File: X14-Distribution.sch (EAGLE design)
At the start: 55 parts, among them Q1 310mA/60V/1.6Ω, Q2 IRF1018EPBF, Q3 IRF1018EPBF, Q4 IRF1018EPBF, Q5 IRLML5203, Q6 IRLML5203, Q7 IRLML5203, Q8 IRLML5203, U1 DIST_OR_CONTROL_ALTMK06A-M, U2 DIST_OR_CONTROL_ALTMK06A-M

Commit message: Changed the Backplane Logic connector
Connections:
- net +12V: no longer U$1.VIN+
- net +12V_CONV: now also BACKPLANE.12V, U$1.VIN+
- net 12V_GND: now also BACKPLANE.GND_12V
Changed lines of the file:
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@@
 <part name="R12" library="SparkFun-Resistors" library_urn="urn:adsk.eagle:library:532" deviceset="RESISTOR" device="0603" package3d_urn="urn:adsk.eagle:package:39650/1" value="10k"/>
 <part name="R13" library="SparkFun-Resistors" library_urn="urn:adsk.eagle:library:532" deviceset="RESISTOR" device="0603" package3d_urn="urn:adsk.eagle:package:39650/1" value="10k"/>
-<part name="BACKPLANE" library="CONN, Distribution-Backplane" deviceset="DISTRIBUTION-BACKPLANE" device=""/>
 <part name="BRICKS1" library="CONN_Distribution-Bricks" deviceset="PETC-02-40-02-01-X-VT(DTOB)" device=""/>
 <part name="BRICKS2" library="CONN_Distribution-Bricks" deviceset="PETC-02-40-02-01-X-VT(DTOB)" device=""/>
@@
 <part name="Q7" library="Transistor" library_urn="urn:adsk.eagle:library:16378713" deviceset="PMOSFET_" device="" package3d_urn="urn:adsk.eagle:package:28738/2" technology="IRLML5203" value="IRLML5203"/>
 <part name="Q8" library="Transistor" library_urn="urn:adsk.eagle:library:16378713" deviceset="PMOSFET_" device="" package3d_urn="urn:adsk.eagle:package:28738/2" technology="IRLML5203" value="IRLML5203"/>
+<part name="BACKPLANE" library="CONN, Distribution-Backplane" deviceset="DISTRIBUTION-BACKPLANE" device="" value=""/>
 </parts>
 <sheets>
@@
 <attribute name="VALUE" x="410.972" y="-129.286" size="1.778" layer="96" font="vector" rot="R90" align="top-center"/>
 </instance>
-<instance part="BACKPLANE" gate="G$1" x="375.158" y="-151.638" smashed="yes">
-<attribute name="NAME" x="366.014" y="-143.002" size="1.778" layer="95"/>
-</instance>
 <instance part="BRICKS1" gate="G$1" x="88.646" y="-138.176" smashed="yes">
 <attribute name="NAME" x="75.946" y="-125.476" size="1.778" layer="95"/>
@@
 <attribute name="NAME" x="261.112" y="82.55" size="1.778" layer="95"/>
 <attribute name="VALUE" x="261.112" y="80.01" size="1.778" layer="96"/>
+</instance>
+<instance part="BACKPLANE" gate="G$1" x="373.634" y="-153.162" smashed="yes">
+<attribute name="NAME" x="363.474" y="-141.732" size="1.778" layer="95"/>
+<attribute name="VALUE" x="363.474" y="-164.592" size="1.778" layer="96" align="top-left"/>
 </instance>
 </instances>
@@
 <label x="442.468" y="81.788" size="1.27" layer="95" xref="yes"/>
 </segment>
-<segment>
-<pinref part="U$1" gate="G$1" pin="VIN+"/>
-<wire x1="74.168" y1="-56.642" x2="66.548" y2="-56.642" width="0.1524" layer="91"/>
-<label x="66.548" y="-56.642" size="1.778" layer="95" rot="R180" xref="yes"/>
-</segment>
 </net>
 <net name="12V_GND" class="0">
@@
 <label x="66.548" y="-61.722" size="1.778" layer="95" rot="R180" xref="yes"/>
 </segment>
+<segment>
+<pinref part="BACKPLANE" gate="G$1" pin="GND_12V"/>
+<wire x1="391.414" y1="-160.782" x2="401.066" y2="-160.782" width="0.1524" layer="91"/>
+<label x="401.066" y="-160.782" size="0.8128" layer="95" xref="yes"/>
+</segment>
 </net>
 <net name="N$5" class="0">
@@
 <pinref part="D12" gate="D$1" pin="2"/>
 </segment>
+<segment>
+<pinref part="U$1" gate="G$1" pin="VIN+"/>
+<wire x1="74.168" y1="-56.642" x2="66.548" y2="-56.642" width="0.1524" layer="91"/>
+<label x="66.548" y="-56.642" size="1.778" layer="95" rot="R180" xref="yes"/>
+</segment>
+<segment>
+<pinref part="BACKPLANE" gate="G$1" pin="12V"/>
+<wire x1="358.394" y1="-160.782" x2="352.044" y2="-160.782" width="0.1524" layer="91"/>
+<label x="352.044" y="-160.782" size="1.778" layer="95" rot="R180" xref="yes"/>
+</segment>
 </net>
 <net name="+5V" class="0">
 <segment>
-<wire x1="361.188" y1="-147.066" x2="354.584" y2="-147.066" width="0.1524" layer="91"/>
-<label x="354.076" y="-147.066" size="1.778" layer="95" rot="R180" xref="yes"/>
+<wire x1="358.394" y1="-145.542" x2="351.79" y2="-145.542" width="0.1524" layer="91"/>
+<label x="351.282" y="-145.542" size="1.778" layer="95" rot="R180" xref="yes"/>
 <pinref part="BACKPLANE" gate="G$1" pin="5V"/>
 </segment>
@@
 <net name="5V_GND" class="0">
 <segment>
-<wire x1="361.188" y1="-157.226" x2="354.584" y2="-157.226" width="0.1524" layer="91"/>
-<label x="354.584" y="-156.972" size="1.778" layer="95" rot="R180" xref="yes"/>
+<wire x1="358.394" y1="-155.702" x2="351.79" y2="-155.702" width="0.1524" layer="91"/>
+<label x="351.79" y="-155.448" size="1.778" layer="95" rot="R180" xref="yes"/>
 <pinref part="BACKPLANE" gate="G$1" pin="GND_5V"/>
 </segment>
@@
 </segment>
 <segment>
-<wire x1="361.188" y1="-152.146" x2="354.584" y2="-152.146" width="0.1524" layer="91"/>
-<label x="354.584" y="-152.146" size="1.778" layer="95" rot="R180" xref="yes"/>
+<wire x1="358.394" y1="-150.622" x2="351.79" y2="-150.622" width="0.1524" layer="91"/>
+<label x="351.79" y="-150.622" size="1.778" layer="95" rot="R180" xref="yes"/>
 <pinref part="BACKPLANE" gate="G$1" pin="3.3V"/>
 </segment>

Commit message: Made some changes for the board
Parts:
- removed DATA_TEST: (no value), SparkFun-Connectors:CONN_02
- removed TETHER: DIST_TO_TETHER, CONN, 6 pin connector to screw connector:DIST_TO_TETHER
- added TETHER_GND, TETHER_POSITIVE: 796636-3, CONN, 3 pin connection to tether:796636-3
- renumbered U$1 to CONVERSION
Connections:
- net 5V_GND renamed D_GND
- net +48V: now also TETHER_POSITIVE.1, TETHER_POSITIVE.2, TETHER_POSITIVE.3; no longer TETHER.4, TETHER.5, TETHER.6
- net CLK: no longer DATA_TEST.1
- net DATA: no longer DATA_TEST.2
- net GND_RAW: now also TETHER_GND.1, TETHER_GND.2, TETHER_GND.3; no longer TETHER.1, TETHER.2, TETHER.3
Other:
- moved on the sheet: ON/OFF_TEST

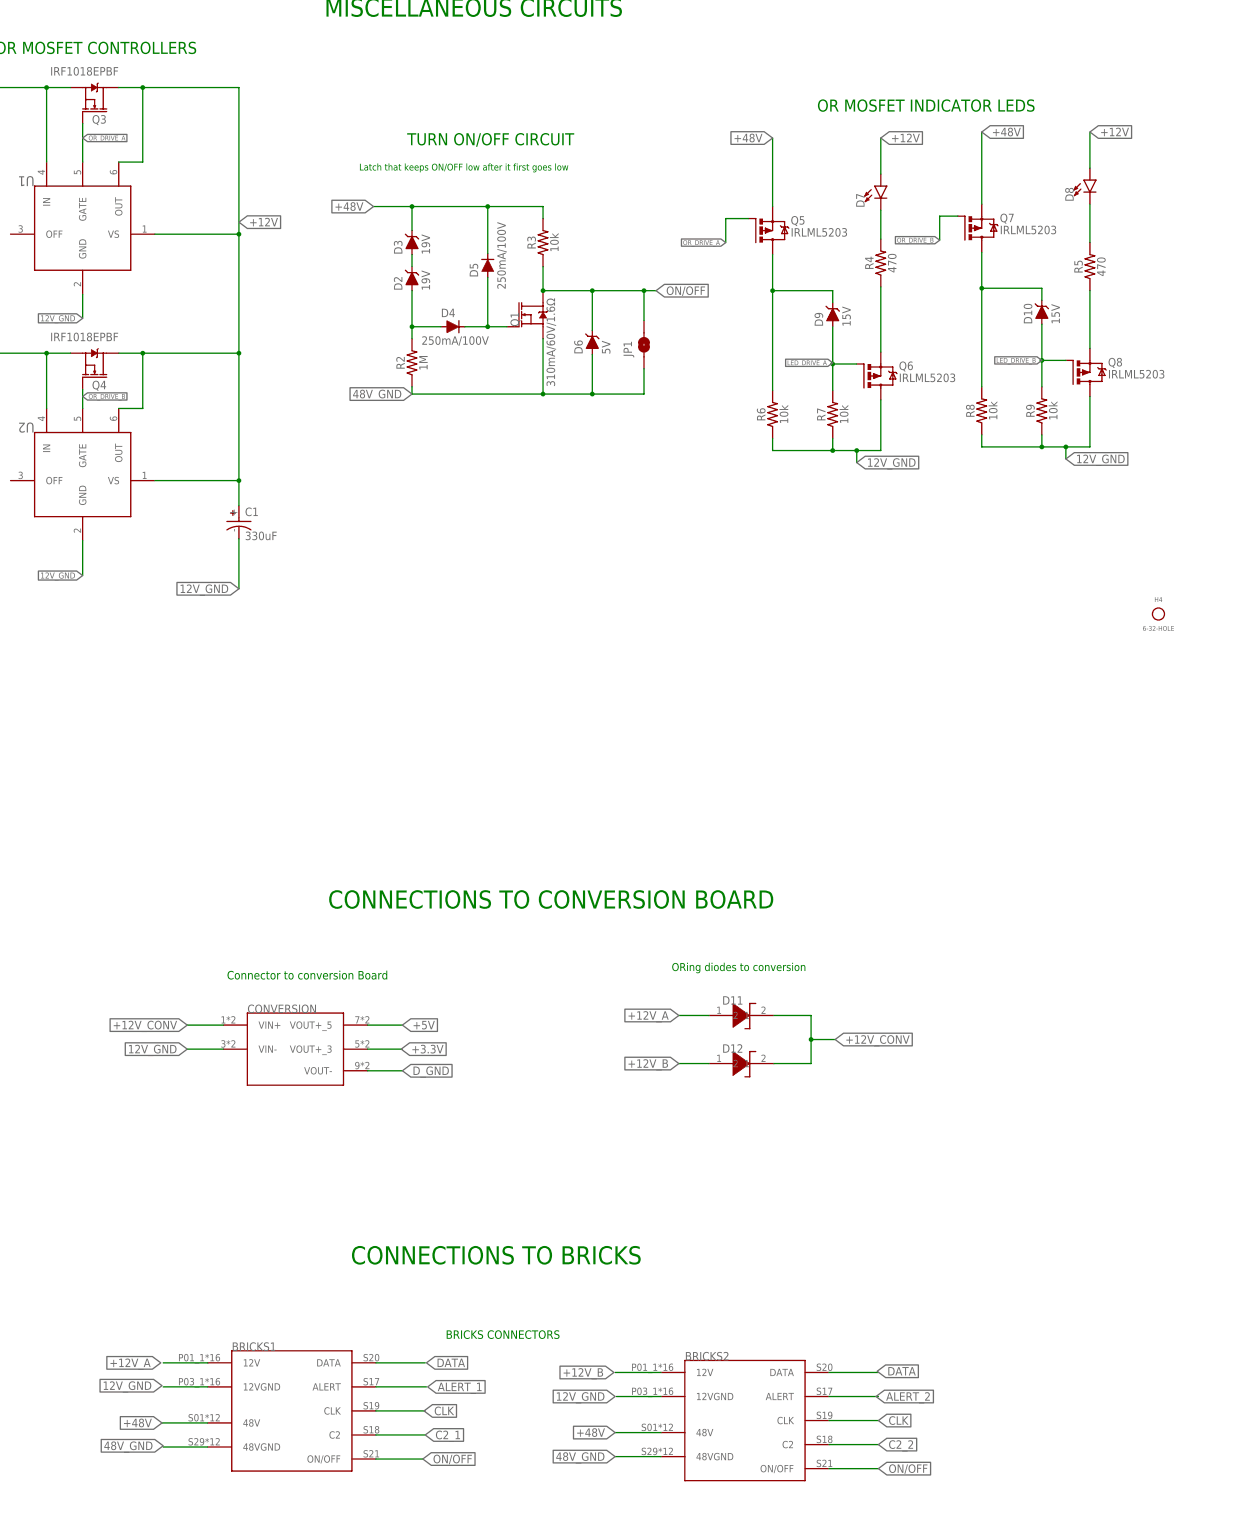
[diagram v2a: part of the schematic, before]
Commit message: Made some changes to board and added 18V zener diodes from 12V_A and B to ground
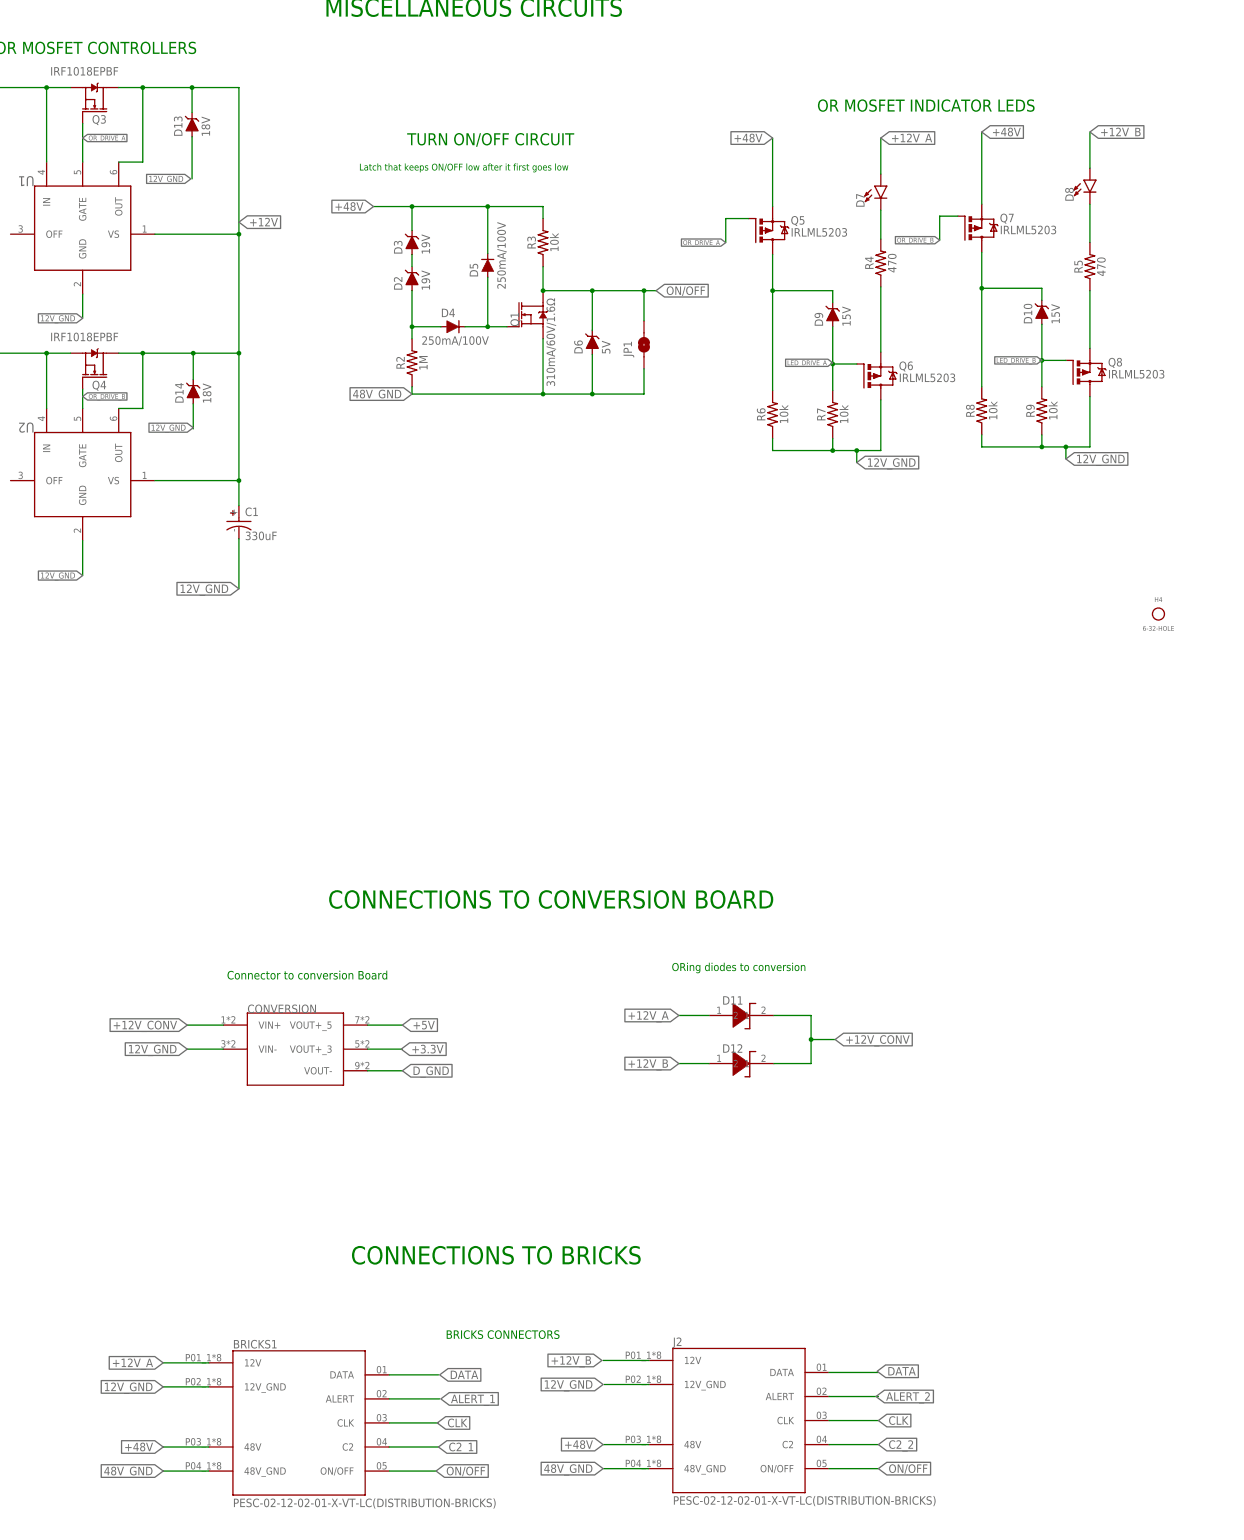
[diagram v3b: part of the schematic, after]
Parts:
- removed BRICKS2: PETC-02-40-02-01-X-VT(DTOB), CONN_Distribution-Bricks:PETC-02-40-02-01-X-VT(DTOB)
- added D13, D14: 18V, SparkFun-DiscreteSemi:DIODE-ZENER-DZ2J150M0L
- added J2: PESC-02-12-02-01-X-VT-LC(DISTRIBUTION-BRICKS), CONN, Distribution-Bricks:PESC-02-12-02-01-X-VT-LC(DISTRIBUTION-BRICKS)
- BRICKS1: value PETC-02-40-02-01-X-VT(DTOB) -> PESC-02-12-02-01-X-VT-LC(DISTRIBUTION-BRICKS); device CONN_Distribution-Bricks:PETC-02-40-02-01-X-VT(DTOB) -> CONN, Distribution-Bricks:PESC-02-12-02-01-X-VT-LC(DISTRIBUTION-BRICKS)
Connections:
- net +12V: now also D13.C, D14.C; no longer D7.A, D8.A
- net +12V_A: now also D7.A
- net +12V_B: now also D8.A, J2.12V; no longer BRICKS2.12V
- net +48V: now also J2.48V; no longer BRICKS2.48V
- net 12V_GND: now also BRICKS1.12V_GND, D13.A, D14.A, J2.12V_GND; no longer BRICKS1.12VGND, BRICKS2.12VGND
- net 48V_GND: now also BRICKS1.48V_GND, J2.48V_GND; no longer BRICKS1.48VGND, BRICKS2.48VGND
- net ALERT_2: now also J2.ALERT; no longer BRICKS2.ALERT
- net C2_2: now also J2.C2; no longer BRICKS2.C2
- net CLK: now also J2.CLK; no longer BRICKS2.CLK
- net DATA: now also J2.DATA; no longer BRICKS2.DATA
- net ON/OFF: now also J2.ON/OFF; no longer BRICKS2.ON/OFF
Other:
- moved on the sheet: BRICKS1
